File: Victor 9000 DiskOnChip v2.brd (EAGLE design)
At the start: 101 x 117.1 mm, 9 parts

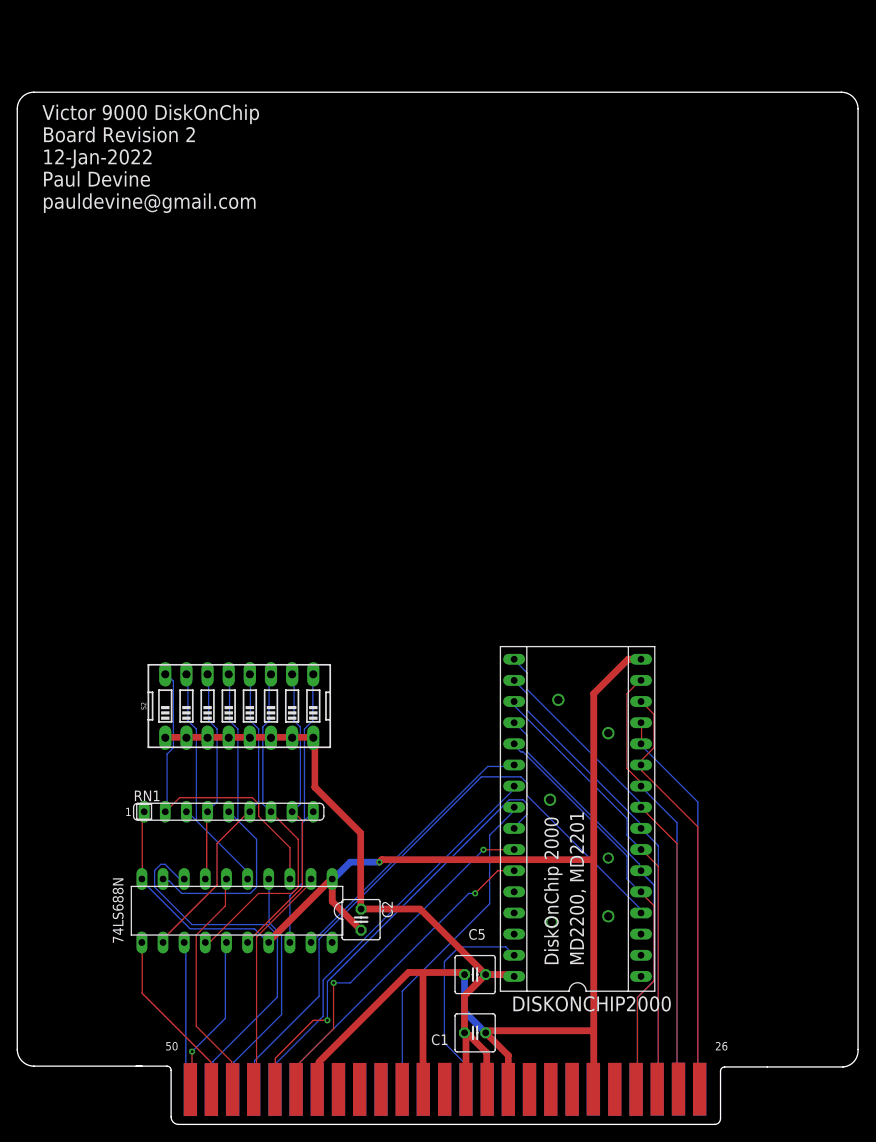
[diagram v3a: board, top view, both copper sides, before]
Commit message: adjusted gold fingers to be slightly thinner to prevent short circuit
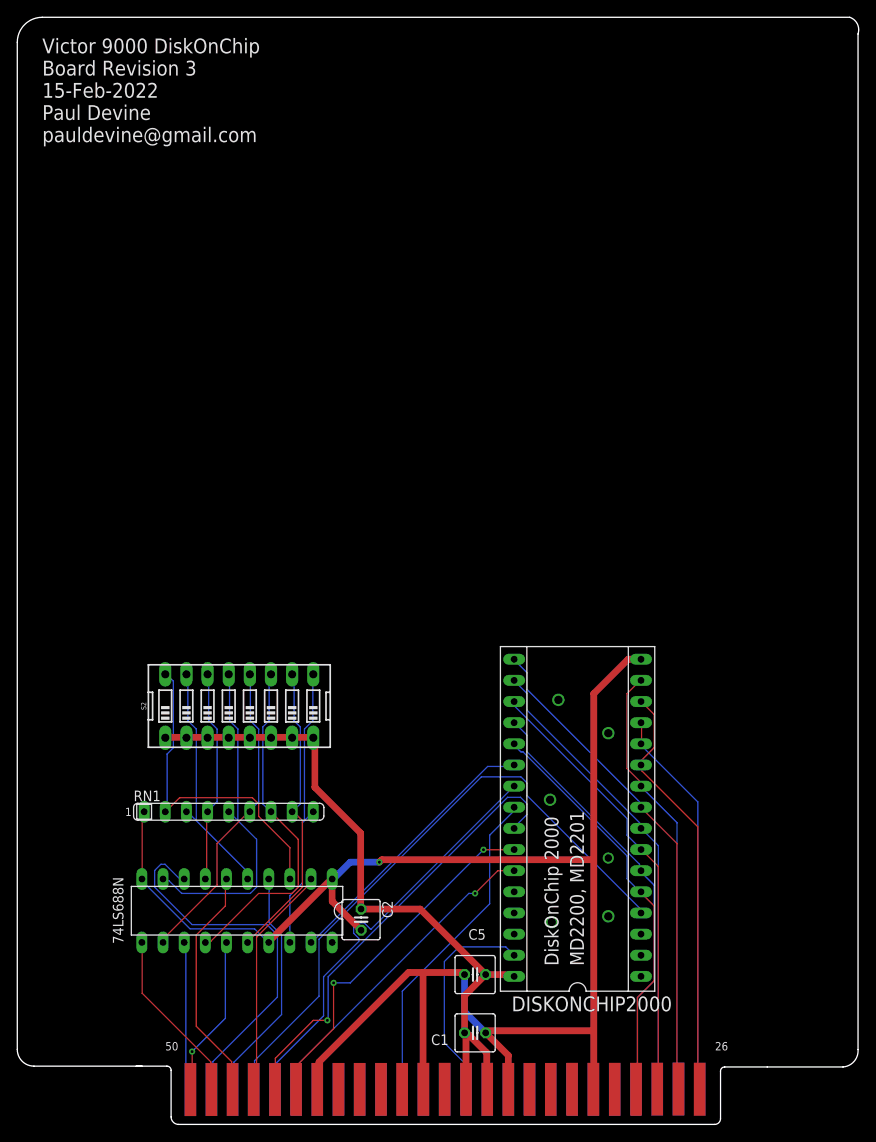
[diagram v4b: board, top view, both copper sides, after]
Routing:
- net A10: track 48.4 -> 50.8 mm
- net GND: track 201.4 -> 203.2 mm
- net A11: track 53.4 -> 53.9 mm
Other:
- board size 101 x 117.1 mm -> 101.1 x 126.1 mm
- board text added: "Victor 9000 DiskOnChip Board Revision 3 15-Feb-2022 Paul Devine pauldevine@gmail.com"
- board text removed: "Victor 9000 DiskOnChip Board Revision 2 12-Jan-2022 Paul Devine pauldevine@gmail.com"
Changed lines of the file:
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@@
 <wire x1="15" y1="7" x2="2" y2="7" width="0.1524" layer="20"/>
 <wire x1="2" y1="7" x2="0" y2="9" width="0.1524" layer="20" curve="-90"/>
-<wire x1="0" y1="9" x2="0" y2="122" width="0.1524" layer="20"/>
-<wire x1="0" y1="122" x2="2" y2="124" width="0.1524" layer="20" curve="-90"/>
-<wire x1="2" y1="124" x2="99" y2="124" width="0.1524" layer="20"/>
-<wire x1="99" y1="124" x2="101" y2="122" width="0.1524" layer="20" curve="-90"/>
-<wire x1="101" y1="122" x2="101" y2="9" width="0.1524" layer="20"/>
+<wire x1="0" y1="9" x2="0" y2="130" width="0.1524" layer="20"/>
+<wire x1="0" y1="130" x2="3" y2="133" width="0.1524" layer="20" curve="-90"/>
+<wire x1="3" y1="133" x2="100" y2="133" width="0.1524" layer="20"/>
+<wire x1="100" y1="133" x2="101" y2="131" width="0.1524" layer="20" curve="-90"/>
+<wire x1="101" y1="131" x2="101" y2="9" width="0.1524" layer="20"/>
 <wire x1="101" y1="9" x2="99.2" y2="6.9" width="0.1524" layer="20" curve="-90"/>
 <wire x1="99.2" y1="6.9" x2="90.1" y2="6.9" width="0.1524" layer="20"/>
-<text x="3" y="110" size="1.778" layer="21" font="vector">Victor 9000 DiskOnChip
-Board Revision 2
-12-Jan-2022
+<text x="3" y="118" size="1.778" layer="21" font="vector">Victor 9000 DiskOnChip
+Board Revision 3
+15-Feb-2022
 Paul Devine
 pauldevine@gmail.com</text>
 <text x="95" y="119" size="1.778" layer="22" font="vector" rot="MR0">TK Add switch to Address values</text>
+<dimension x1="3" y1="7" x2="3" y2="133" x3="-7" y3="70" textsize="1.778" layer="48"/>
 </plain>
 <attributes>
@@
 <wire x1="38" y1="29.25" x2="37.83" y2="29.48" width="0.1524" layer="1"/>
 <wire x1="47" y1="18.25" x2="48.75" y2="18.25" width="0.8128" layer="1"/>
-<wire x1="48.75" y1="18.25" x2="53.75" y2="18.25" width="0.8128" layer="1"/>
+<wire x1="48.75" y1="18.25" x2="52" y2="18.25" width="0.8128" layer="1"/>
+<wire x1="52" y1="18.25" x2="53.75" y2="18.25" width="0.8128" layer="1"/>
 <wire x1="37.75" y1="29.5" x2="30.25" y2="22" width="0.8128" layer="1"/>
 <wire x1="30.25" y1="22" x2="30.21" y2="21.86" width="0.1524" layer="1"/>
@@
 <wire x1="58.989" y1="4.207" x2="58.989" y2="8.281" width="0.8128" layer="1"/>
 <wire x1="58.989" y1="8.281" x2="56.27" y2="11" width="0.8128" layer="1"/>
-<wire x1="53.75" y1="18.25" x2="53.73" y2="18" width="0" layer="19" extent="1-1"/>
+<wire x1="53.73" y1="18" x2="52.25" y2="18" width="0.1524" layer="1"/>
+<wire x1="52.25" y1="18" x2="52" y2="18.25" width="0.1524" layer="1"/>
 </signal>
 <signal name="VCC">
@@
 <contactref element="DISKONCHIP2000" pad="23"/>
 <contactref element="U$1" pad="A10"/>
-<wire x1="59.69" y1="40.64" x2="59.69" y2="40.29" width="0.1524" layer="16"/>
-<wire x1="59.69" y1="40.29" x2="36.75" y2="17.35" width="0.1524" layer="16"/>
-<wire x1="36.75" y1="13" x2="36.75" y2="17.35" width="0.1524" layer="16"/>
-<wire x1="31" y1="7.25" x2="36.75" y2="13" width="0.1524" layer="16"/>
+<wire x1="59.69" y1="40.64" x2="42.525" y2="23.475" width="0.1524" layer="16"/>
+<wire x1="41.025" y1="21.975" x2="36.796153125" y2="17.746153125" width="0.1524" layer="16"/>
+<wire x1="36.796153125" y1="13.046153125" x2="36.796153125" y2="17.746153125" width="0.1524" layer="16"/>
+<wire x1="31" y1="7.25" x2="36.796153125" y2="13.046153125" width="0.1524" layer="16"/>
 <wire x1="31" y1="4.25" x2="31" y2="7.25" width="0.1524" layer="16"/>
 <wire x1="31" y1="4.25" x2="30.947" y2="4.191" width="0.1524" layer="16"/>
+<wire x1="41.6682375" y1="24.219" x2="40.9317625" y2="24.219" width="0.1524" layer="16"/>
+<wire x1="40.9317625" y1="24.219" x2="40.411" y2="23.6982375" width="0.1524" layer="16"/>
+<wire x1="40.411" y1="23.6982375" x2="40.411" y2="22.9617625" width="0.1524" layer="16"/>
+<wire x1="42.525" y1="23.475" x2="42.4122375" y2="23.475" width="0.1524" layer="16"/>
+<wire x1="40.411" y1="22.9617625" x2="41.025" y2="22.3477625" width="0.1524" layer="16"/>
+<wire x1="41.025" y1="22.3477625" x2="41.025" y2="21.975" width="0.1524" layer="16"/>
+<wire x1="42.4122375" y1="23.475" x2="41.6682375" y2="24.219" width="0.1524" layer="16"/>
 </signal>
 <signal name="A12">
@@
 <wire x1="61.25" y1="37.25" x2="59.75" y2="35.75" width="0.1524" layer="16"/>
 <wire x1="61.25" y1="38.5" x2="61.25" y2="37.25" width="0.1524" layer="16"/>
-<wire x1="60.75" y1="39" x2="61.25" y2="38.5" width="0.1524" layer="16"/>
-<wire x1="59.1" y1="39" x2="60.75" y2="39" width="0.1524" layer="16"/>
-<wire x1="37.25" y1="17.15" x2="59.1" y2="39" width="0.1524" layer="16"/>
-<wire x1="37.25" y1="12.5" x2="37.25" y2="17.15" width="0.1524" layer="16"/>
+<wire x1="60.45" y1="39.3" x2="61.25" y2="38.5" width="0.1524" layer="16"/>
+<wire x1="58.9" y1="39.3" x2="60.45" y2="39.3" width="0.1524" layer="16"/>
+<wire x1="37.35" y1="17.75" x2="58.9" y2="39.3" width="0.1524" layer="16"/>
+<wire x1="37.25" y1="12.5" x2="37.35" y2="12.6" width="0.1524" layer="16"/>
+<wire x1="37.35" y1="17.75" x2="37.35" y2="12.6" width="0.1524" layer="16"/>
 <wire x1="35.55" y1="12.5" x2="31" y2="7.95" width="0.1524" layer="1"/>
 <wire x1="35.55" y1="12.5" x2="37.25" y2="12.5" width="0.1524" layer="1"/>
